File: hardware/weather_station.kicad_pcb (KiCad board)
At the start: 4 copper layers, 85.4 x 36.4 mm, 70 parts, among them J1 USB_MICRO, Q1 BD135, Q2 BD135, SW1 SWITCH_SPDT, U1 nRF51x22, U2 TMP112, U3 BMP280, U4 Si7013, U5 LM3668, U6 MCP73831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

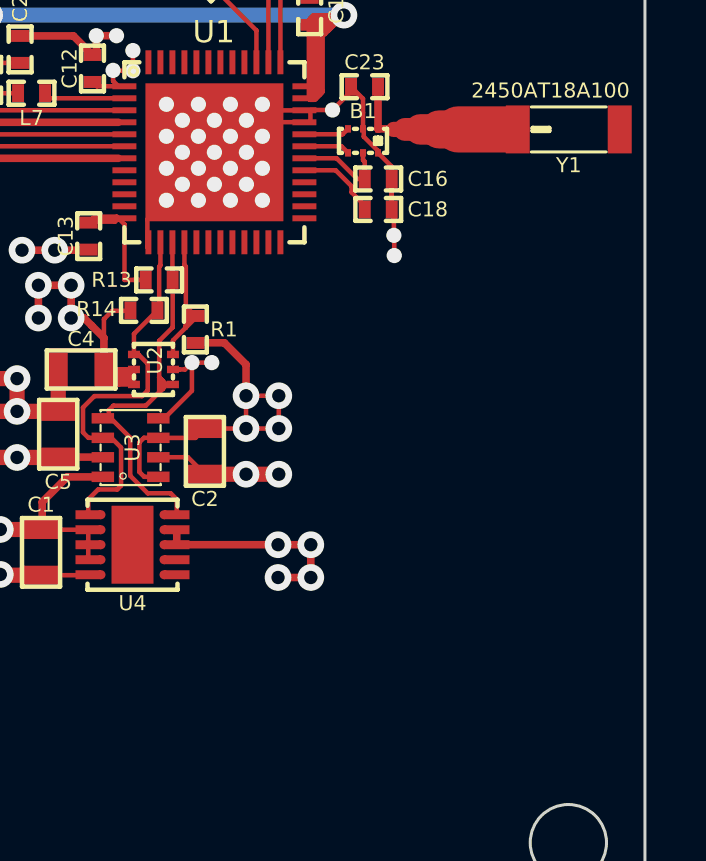
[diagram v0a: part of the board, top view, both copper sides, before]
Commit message: Add footprint for headers and route
Add a 1.27mm pitched footprint for headers, add them to the pcb and route.
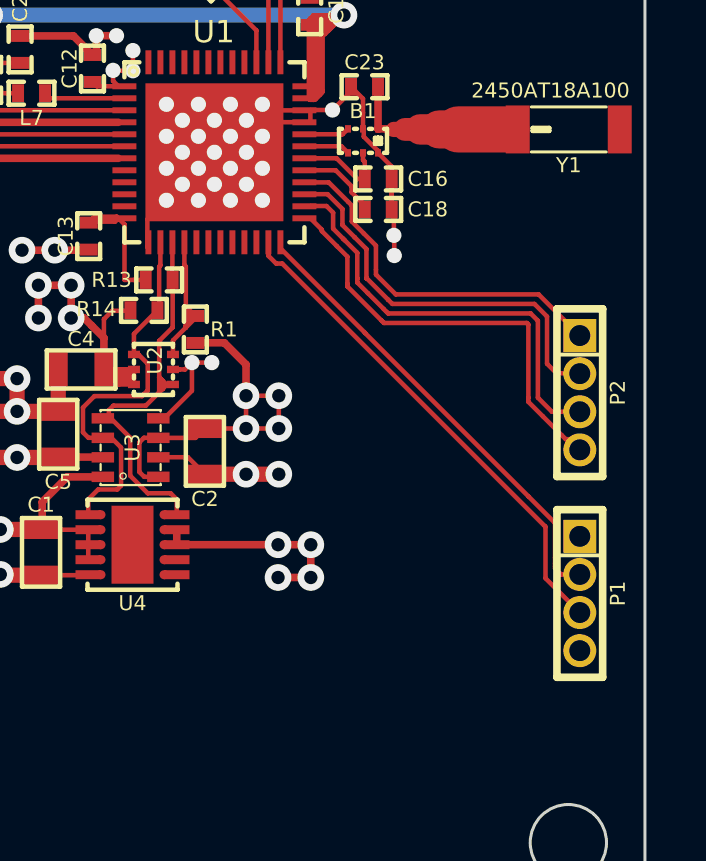
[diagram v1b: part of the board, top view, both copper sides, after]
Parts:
- added P1: CONN_01X04, weather:4PIN_1.27MMP, F.Cu at (259.7, 56.2)
- added P2: CONN_01X04, weather:4PIN_1.27MMP, F.Cu at (259.7, 49.5)
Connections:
- U1 pad 23: Net-(U1-Pad23) -> SWDIO
- U1 pad 24: Net-(U1-Pad24) -> SWDCLK
- U1 pad 25: Net-(U1-Pad25) -> P0.17
- U1 pad 26: Net-(U1-Pad26) -> P0.18
- U1 pad 27: Net-(U1-Pad27) -> P0.19
- U1 pad 28: Net-(U1-Pad28) -> P0.20
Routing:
- net SWDIO: track 0.00 -> 16.6 mm
- net SWDCLK: track 0.00 -> 15.4 mm
- net P0.18: track 0.00 -> 14.3 mm
- net P0.17: track 0.00 -> 14.3 mm
- net P0.19: track 0.00 -> 13.3 mm
- net P0.20: track 0.00 -> 12.0 mm
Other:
- board text added: "PGM"

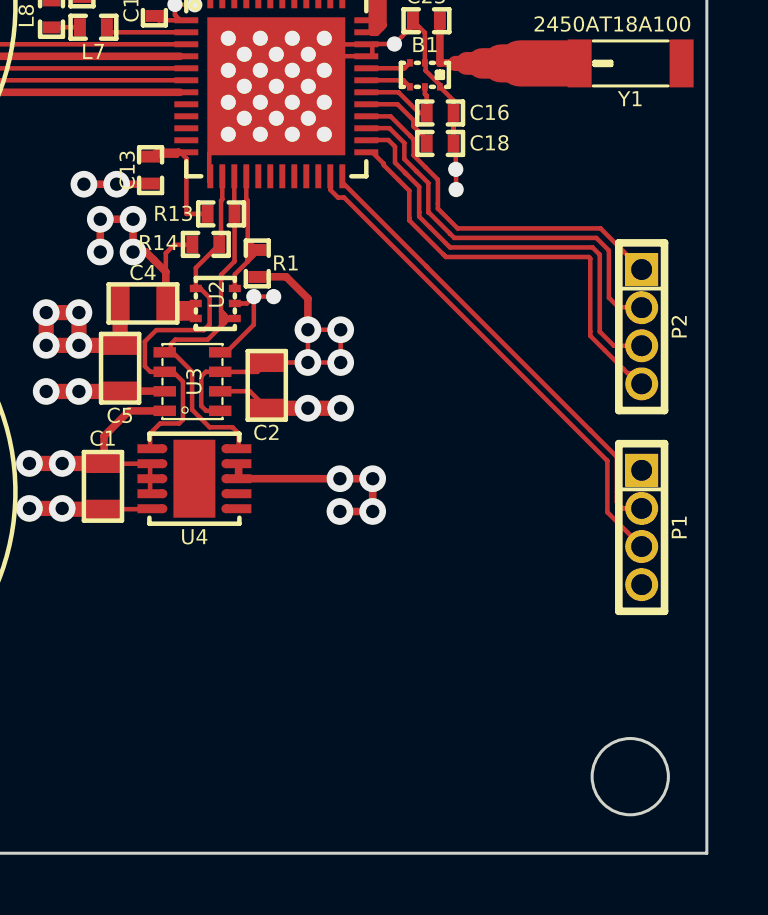
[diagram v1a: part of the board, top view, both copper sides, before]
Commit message: Add header and route the south side gpio's
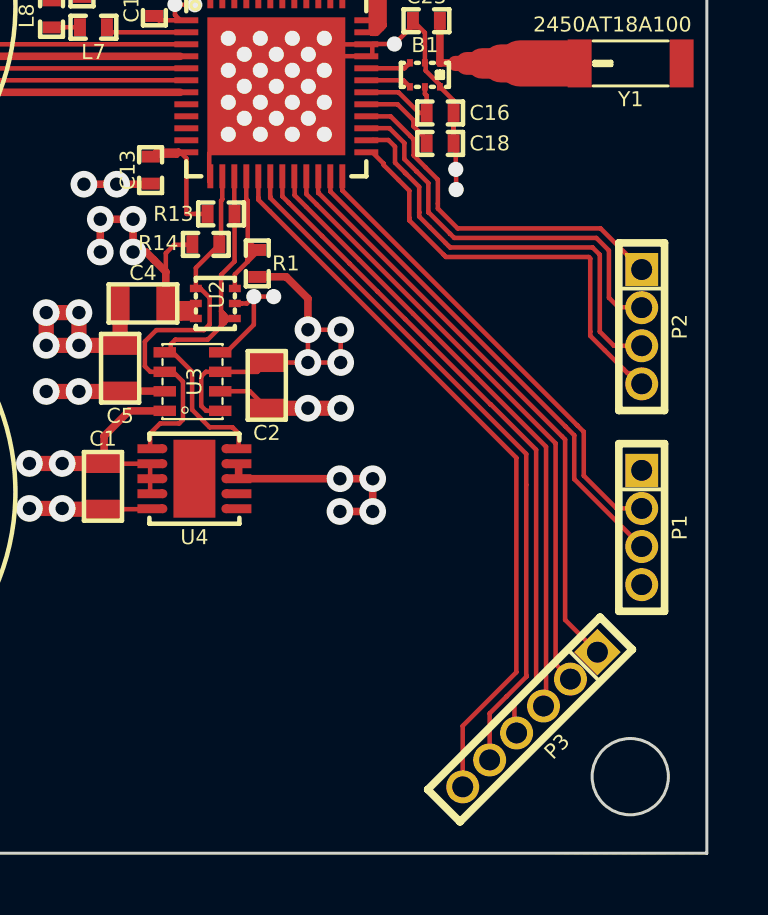
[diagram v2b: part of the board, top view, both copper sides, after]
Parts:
- added P3: CONN_01X06, weather:6PIN_1.27MMP, F.Cu at (256.0, 62.6)
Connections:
- U1 pad : GND -> (no net)
- U1 pad 17: Net-(U1-Pad17) -> P0.11
- U1 pad 18: Net-(U1-Pad18) -> P0.12
- U1 pad 19: Net-(U1-Pad19) -> P0.13
- U1 pad 20: Net-(U1-Pad20) -> P0.14
- U1 pad 21: Net-(U1-Pad21) -> P0.15
- U1 pad 22: Net-(U1-Pad22) -> P0.16
- U5 pad ~: GND -> (no net)
- U7 pad ~: GND -> (no net)
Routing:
- net P0.11: track 0.00 -> 24.5 mm
- net P0.12: track 0.00 -> 23.3 mm
- net P0.13: track 0.00 -> 22.2 mm
- net P0.14: track 0.00 -> 21.0 mm
- net P0.15: track 0.00 -> 20.5 mm
- net P0.16: track 0.00 -> 19.5 mm
- net (no net): track 0.00 -> 8.67 mm, vias 0 -> 10
- net GND: track 195.0 -> 186.4 mm, vias 115 -> 105

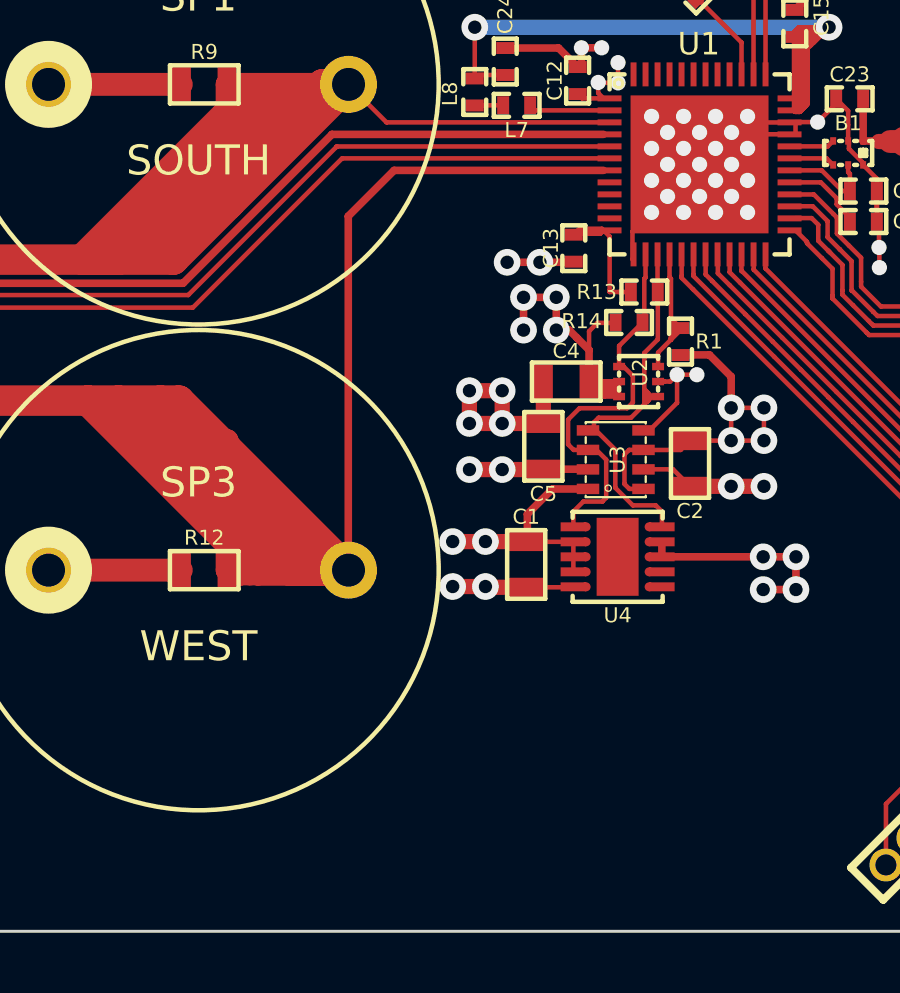
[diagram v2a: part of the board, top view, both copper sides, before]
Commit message: Add footprint and route west side GPIO's
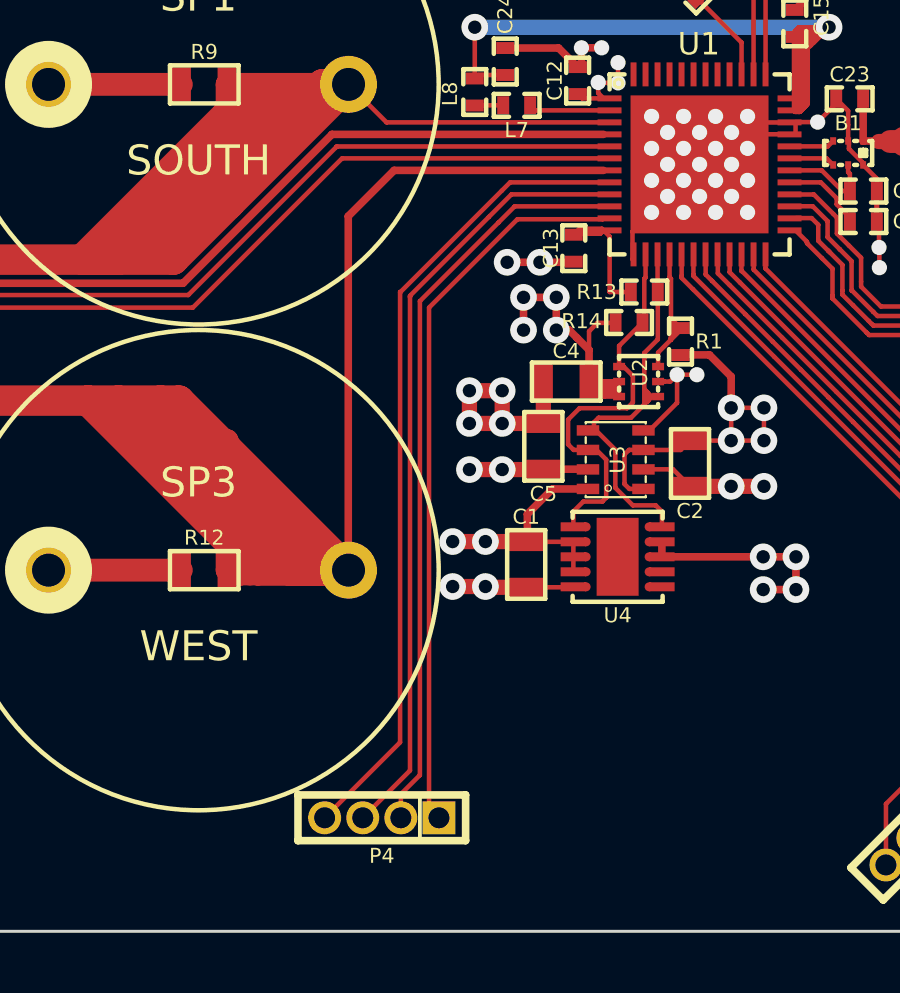
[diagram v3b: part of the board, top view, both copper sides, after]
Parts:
- added P4: CONN_01X04, weather:4PIN_1.27MMP, F.Cu at (236.9, 63.3)
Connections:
- U1 pad : (no net) -> GND
- U1 pad 10: Net-(U1-Pad10) -> P0.06
- U1 pad 11: Net-(U1-Pad11) -> P0.07
- U1 pad 8: Net-(U1-Pad8) -> P0.04
- U1 pad 9: Net-(U1-Pad9) -> P0.05
- U5 pad ~: (no net) -> GND
- U7 pad ~: (no net) -> GND
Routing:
- net P0.04: track 0.00 -> 26.9 mm
- net P0.05: track 0.00 -> 25.9 mm
- net P0.06: track 0.00 -> 24.9 mm
- net P0.07: track 0.00 -> 24.2 mm
- net (no net): track 8.67 -> 0.00 mm, vias 10 -> 0
- net GND: track 186.4 -> 195.0 mm, vias 105 -> 115

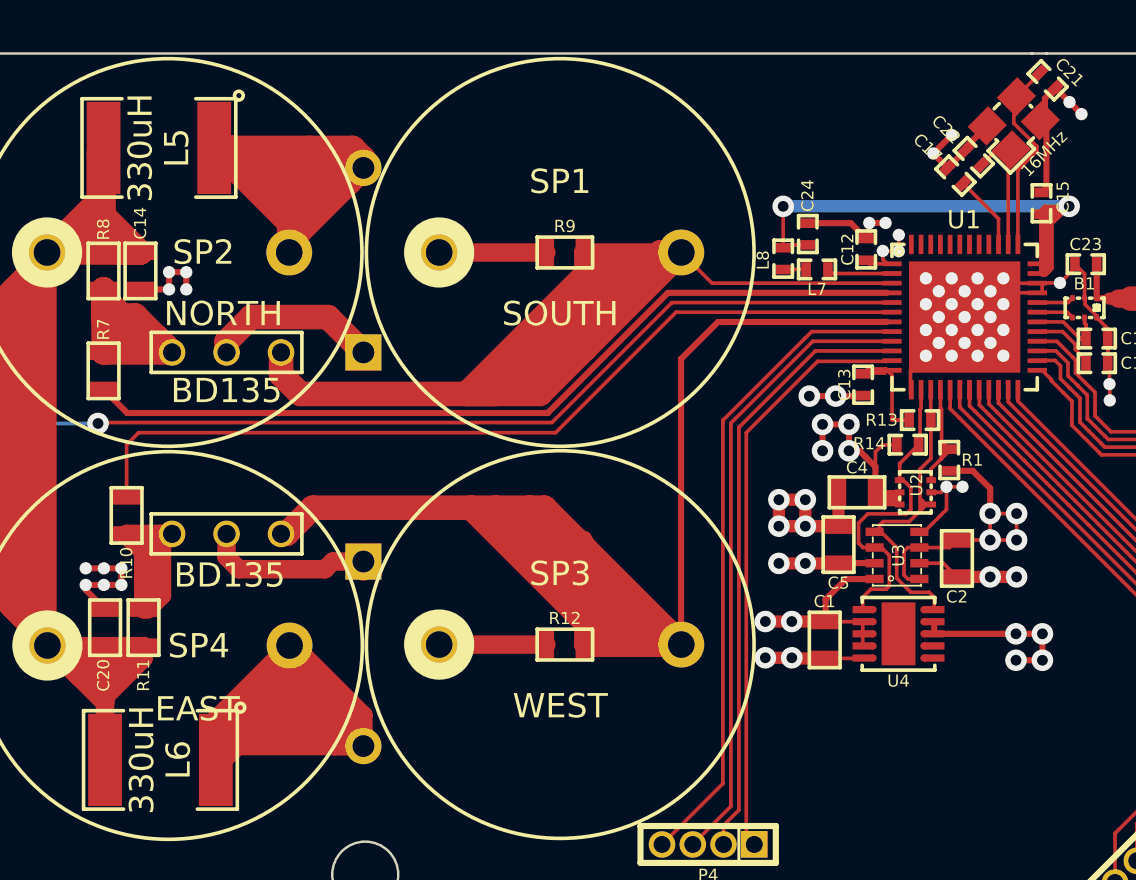
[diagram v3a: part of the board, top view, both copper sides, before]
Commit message: Add footprint for northside gpio's and routing
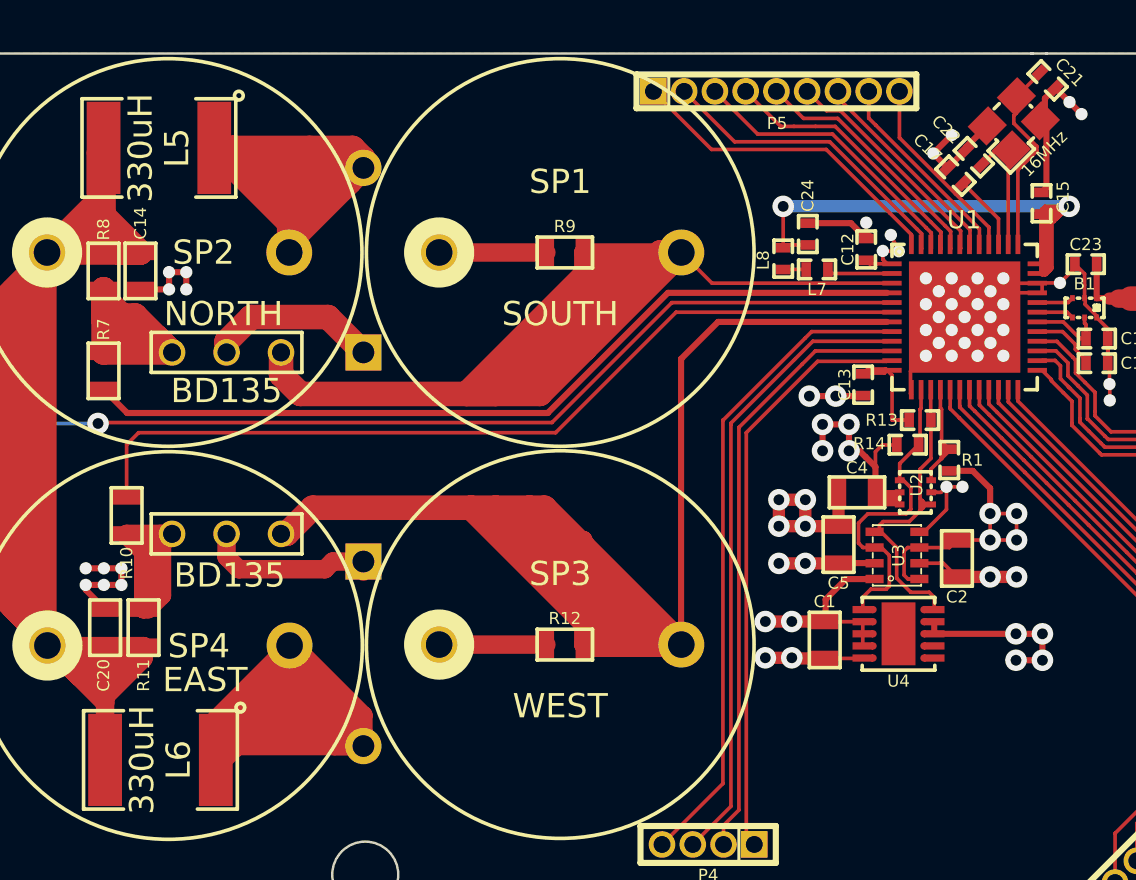
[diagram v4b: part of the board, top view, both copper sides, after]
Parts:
- added P5: CONN_01X09, weather:9PIN_1.27MMP, F.Cu at (239.8, 32.2)
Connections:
- U1 pad 40: Net-(U1-Pad40) -> P0.21
- U1 pad 41: Net-(U1-Pad41) -> P0.22
- U1 pad 42: Net-(U1-Pad42) -> P0.23
- U1 pad 43: Net-(U1-Pad43) -> P0.24
- U1 pad 44: Net-(U1-Pad44) -> P0.25
- U1 pad 45: Net-(U1-Pad45) -> P0.26
- U1 pad 46: Net-(U1-Pad46) -> P0.27
- U1 pad 47: Net-(U1-Pad47) -> P0.28
- U1 pad 48: Net-(U1-Pad48) -> P0.29
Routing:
- net P0.29: track 0.00 -> 13.7 mm
- net P0.28: track 0.00 -> 12.9 mm
- net P0.27: track 0.00 -> 12.0 mm
- net P0.26: track 0.00 -> 11.2 mm
- net P0.25: track 0.00 -> 10.3 mm
- net P0.24: track 0.00 -> 9.50 mm
- net P0.23: track 0.00 -> 8.80 mm
- net P0.22: track 0.00 -> 8.42 mm
- net P0.21: track 0.00 -> 8.05 mm
- net GND: track 195.0 -> 194.6 mm, vias 115 -> 114

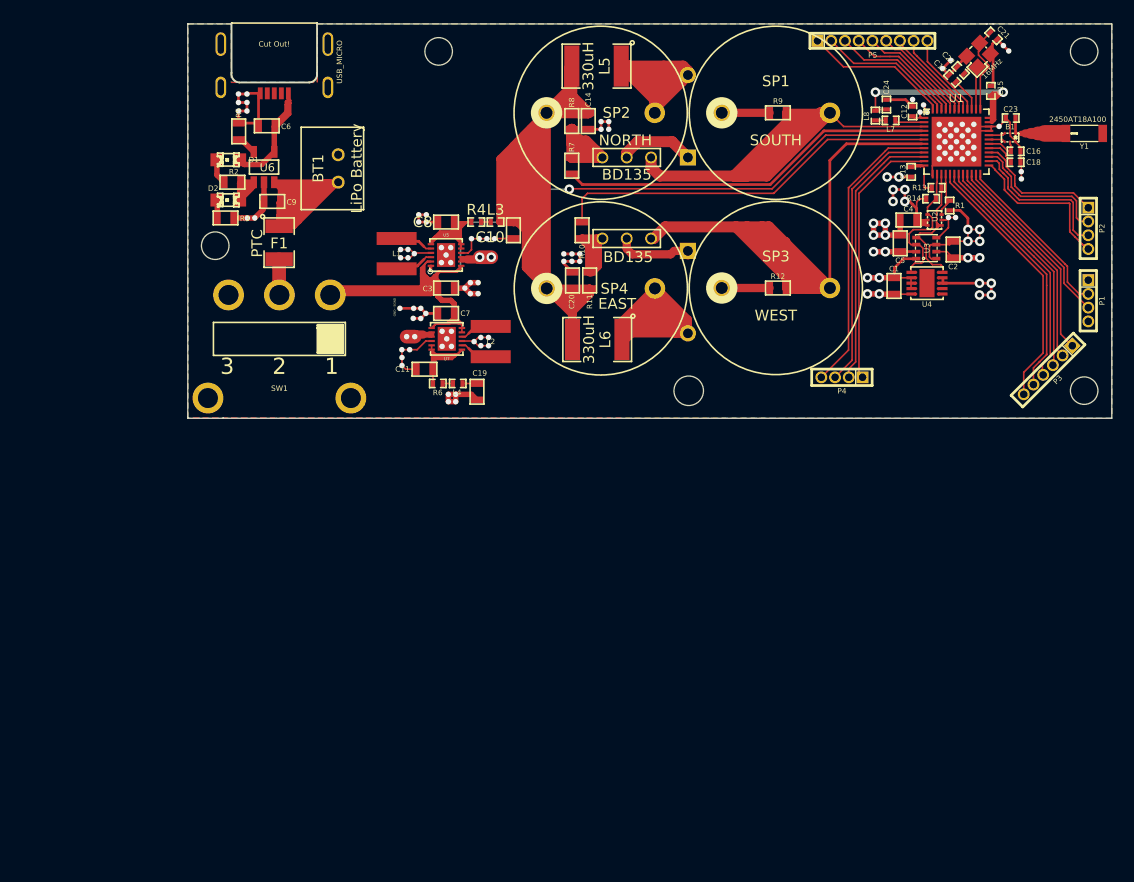
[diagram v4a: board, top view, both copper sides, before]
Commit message: Reroute entire PCB
Smaller, faster, better.. Pick one of 2 ;)
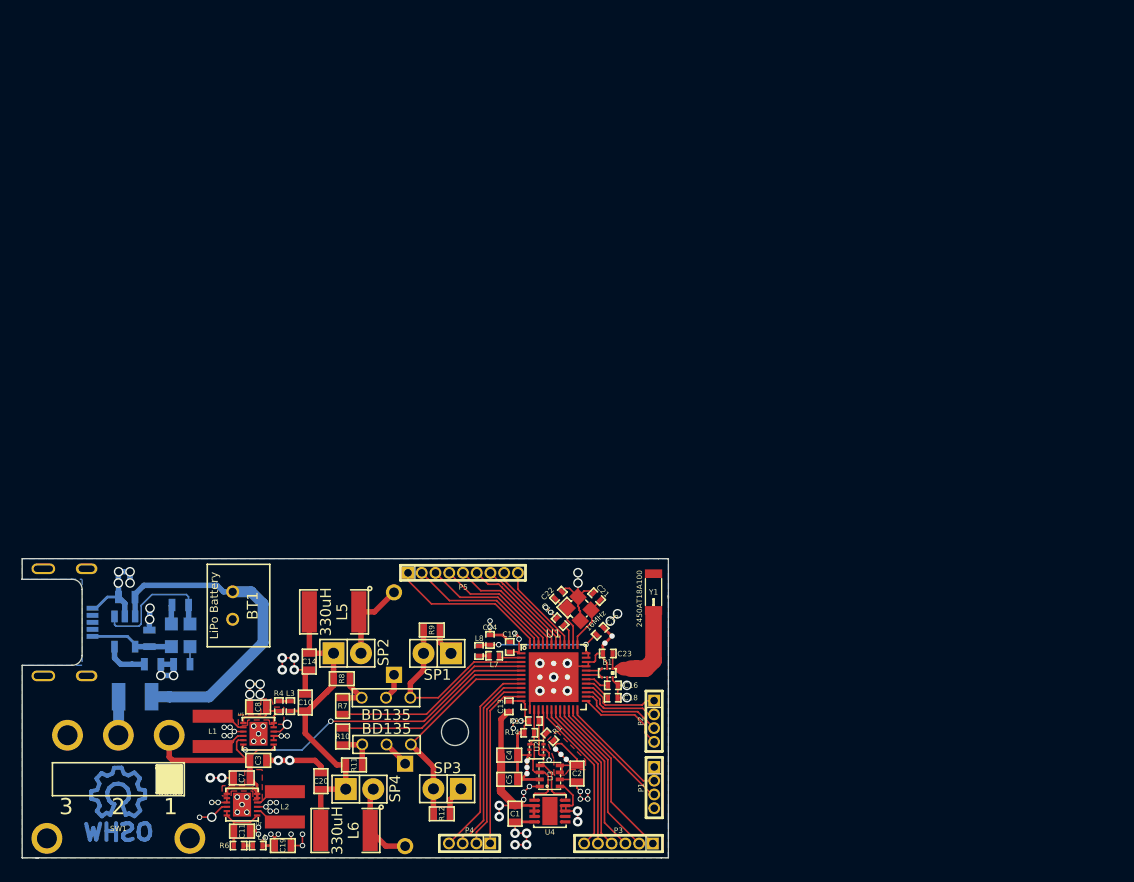
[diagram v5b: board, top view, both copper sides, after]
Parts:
- added MountingHole_2-5mm: VAL**, Mounting_Holes:MountingHole_2-5mm, F.Cu at (201.2, 96.1)
- added Symbol_OSHW-Logo_CopperTop: VAL**, Symbols:Symbol_OSHW-Logo_CopperTop, B.Cu at (170.0, 101.9)
- C6, C9, D1, D2, F1, J1, R2, R3, R5, U6: moved to B.Cu
- SP1, SP2, SP3, SP4: footprint weather:ULTRASONIC_MCUST16A40S12RO -> Pin_Headers:Pin_Header_Straight_1x02
- moved C21 63.5 mm to (214.3, 83.6), turned to 135 degrees
- moved X1 63.1 mm to (212.6, 84.7), turned to 315 degrees
- moved P5 62.1 mm to (201.9, 81.4)
- moved C17 61.9 mm to (210.9, 85.9)
- moved C12 61.9 mm to (206.2, 88.2)
- moved C18 61.9 mm to (215.7, 92.9)
- moved C23 61.9 mm to (215.3, 88.8)
- moved B1 61.9 mm to (215.2, 90.6)
- moved U1 61.9 mm to (210.3, 91.0)
- moved C13 61.8 mm to (206.1, 93.7)
- moved C16 61.8 mm to (215.8, 91.8)
- moved R14 61.8 mm to (208.0, 96.2)
- moved R13 61.8 mm to (208.5, 95.1)
- moved C4 61.7 mm to (206.2, 98.2)
- moved C15 61.6 mm to (214.6, 86.8), turned to 45 degrees
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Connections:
- U3 pad 5: GND -> V3.3
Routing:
- net V5.0: track 179.5 -> 33.4 mm
- net PULSE2: track 104.9 -> 19.8 mm
- net VIN: track 81.2 -> 23.2 mm
- net Net-(D4-Pad1): track 65.4 -> 7.76 mm
- net PULSE1: track 64.4 -> 18.2 mm
- net Net-(C8-Pad1): track 50.6 -> 6.42 mm
- net GND: track 194.6 -> 158.7 mm, vias 114 -> 83
- net Net-(D3-Pad1): track 34.9 -> 7.91 mm
- net V50_EN: track 53.3 -> 28.9 mm
- net VBAT: track 54.6 -> 30.9 mm
- net AVDD: track 33.5 -> 12.6 mm
- net Net-(C11-Pad1): track 24.7 -> 5.88 mm
- net PWM2: track 35.8 -> 18.3 mm
- net PWM1: track 34.8 -> 18.1 mm
- net Net-(C6-Pad1): track 18.3 -> 7.83 mm
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- added copper zone on F.Cu, net Net-(C8-Pad1)
- added copper zone on F.Cu, net VIN
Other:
- board size 85.4 x 36.4 mm -> 59.7 x 27.6 mm
- board text removed: "GND - SGND"
- board text removed: "PGM"
